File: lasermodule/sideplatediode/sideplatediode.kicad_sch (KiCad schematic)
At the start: 4 parts, among them J1 Conn_01x02

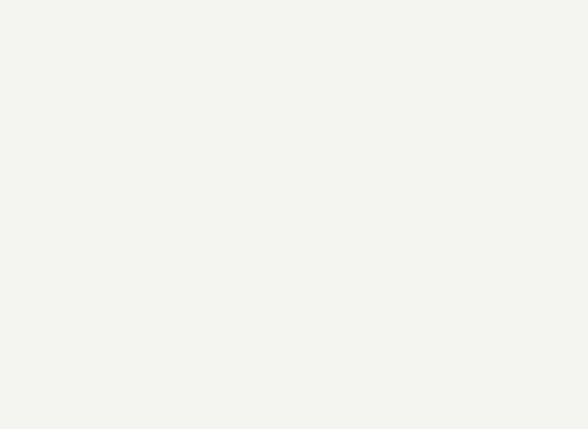
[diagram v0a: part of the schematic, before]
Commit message: removed need for screws using pcb pads
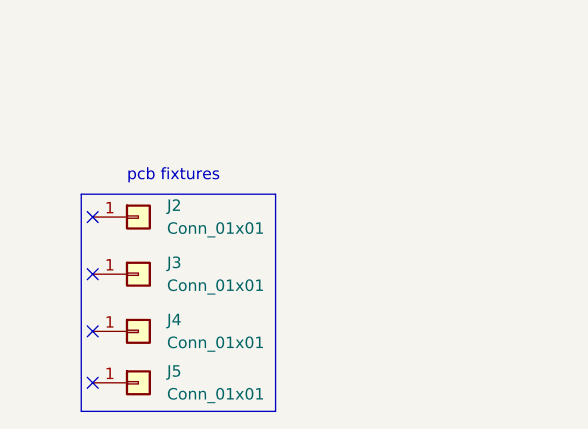
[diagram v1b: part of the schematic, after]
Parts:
- added J2, J3, J4, J5: Conn_01x01, start-of-scanline-detector:TestPoint_Pad_2.0x2.0mm_nosilk, symbol Connector_Generic:Conn_01x01
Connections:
- no-connect marks 0 -> 4
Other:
- note added: "pcb fixtures"
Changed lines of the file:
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@@
     (comment 1 "Author: Rik Starmans")
   )
+  (no_connect (at 51.435 112.395))
+  (no_connect (at 51.435 118.11))
+  (no_connect (at 51.435 106.045))
+  (no_connect (at 51.435 99.695))
+  (polyline (pts (xy 50.165 97.155) (xy 71.755 97.155))
+    (stroke (width 0) (type default))
+  )
   (wire (pts (xy 58.42 52.07) (xy 58.42 41.91))
     (stroke (width 0) (type default))
@@
     (stroke (width 0) (type default))
   )
+  (polyline (pts (xy 50.165 121.285) (xy 71.755 121.285))
+    (stroke (width 0) (type default))
+  )
   (wire (pts (xy 53.34 52.07) (xy 58.42 52.07))
     (stroke (width 0) (type default))
@@
     (stroke (width 0) (type default))
   )
+  (polyline (pts (xy 50.165 97.155) (xy 50.165 121.285))
+    (stroke (width 0) (type default))
+  )
+  (polyline (pts (xy 71.755 121.285) (xy 71.755 97.155))
+    (stroke (width 0) (type default))
+  )
   (text "back" (at 110.49 62.23 0)
+    (effects (font (size 1.27 1.27)) (justify left bottom))
+  )
+  (text "pcb fixtures" (at 55.245 95.885 0)
     (effects (font (size 1.27 1.27)) (justify left bottom))
   )
@@
     )
   )
+  (symbol (lib_id "Connector_Generic:Conn_01x01") (at 56.515 112.395 0) (unit 1)
+    (in_bom yes) (on_board yes) (dnp no) (fields_autoplaced)
+    (property "Reference" "J4" (at 59.69 111.125 0)
+      (effects (font (size 1.27 1.27)) (justify left))
+    )
+    (property "Value" "Conn_01x01" (at 59.69 113.665 0)
+      (effects (font (size 1.27 1.27)) (justify left))
+    )
+    (property "Footprint" "start-of-scanline-detector:TestPoint_Pad_2.0x2.0mm_nosilk" (at 56.515 112.395 0)
+      (effects (font (size 1.27 1.27)) hide)
+    )
+    (property "Datasheet" "~" (at 56.515 112.395 0)
+      (effects (font (size 1.27 1.27)) hide)
+    )
+    (pin "1")
+    (instances
+      (project "sideplatediode"
+        (path "/0f31f11f-c374-4640-b9a4-07bbdba8d354"
+          (reference "J4") (unit 1)
+        )
+      )
+    )
+  )
   (symbol (lib_id "Graphic:Logo_Open_Hardware_Small") (at 92.71 68.58 0) (unit 1)
     (in_bom no) (on_board yes) (dnp no) (fields_autoplaced)
@@
         )
       )
+    )
+  )
+  (symbol (lib_id "Connector_Generic:Conn_01x01") (at 56.515 118.11 0) (unit 1)
+    (in_bom yes) (on_board yes) (dnp no) (fields_autoplaced)
+    (property "Reference" "J5" (at 59.69 116.84 0)
+      (effects (font (size 1.27 1.27)) (justify left))
+    )
+    (property "Value" "Conn_01x01" (at 59.69 119.38 0)
+      (effects (font (size 1.27 1.27)) (justify left))
+    )
+    (property "Footprint" "start-of-scanline-detector:TestPoint_Pad_2.0x2.0mm_nosilk" (at 56.515 118.11 0)
+      (effects (font (size 1.27 1.27)) hide)
+    )
+    (property "Datasheet" "~" (at 56.515 118.11 0)
+      (effects (font (size 1.27 1.27)) hide)
+    )
+    (pin "1")
+    (instances
+      (project "sideplatediode"
+        (path "/0f31f11f-c374-4640-b9a4-07bbdba8d354"
+          (reference "J5") (unit 1)
+        )
+      )
+    )
+  )
+  (symbol (lib_id "Connector_Generic:Conn_01x01") (at 56.515 106.045 0) (unit 1)
+    (in_bom yes) (on_board yes) (dnp no) (fields_autoplaced)
+    (property "Reference" "J3" (at 59.69 104.775 0)
+      (effects (font (size 1.27 1.27)) (justify left))
+    )
+    (property "Value" "Conn_01x01" (at 59.69 107.315 0)
+      (effects (font (size 1.27 1.27)) (justify left))
+    )
+    (property "Footprint" "start-of-scanline-detector:TestPoint_Pad_2.0x2.0mm_nosilk" (at 56.515 106.045 0)
+      (effects (font (size 1.27 1.27)) hide)
+    )
+    (property "Datasheet" "~" (at 56.515 106.045 0)
+      (effects (font (size 1.27 1.27)) hide)
+    )
+    (pin "1")
+    (instances
+      (project "sideplatediode"
+        (path "/0f31f11f-c374-4640-b9a4-07bbdba8d354"
+          (reference "J3") (unit 1)
+        )
+      )
+    )
+  )
+  (symbol (lib_id "Connector_Generic:Conn_01x01") (at 56.515 99.695 0) (unit 1)
+    (in_bom yes) (on_board yes) (dnp no) (fields_autoplaced)
+    (property "Reference" "J2" (at 59.69 98.425 0)
+      (effects (font (size 1.27 1.27)) (justify left))
+    )
+    (property "Value" "Conn_01x01" (at 59.69 100.965 0)
+      (effects (font (size 1.27 1.27)) (justify left))
+    )
+    (property "Footprint" "start-of-scanline-detector:TestPoint_Pad_2.0x2.0mm_nosilk" (at 56.515 99.695 0)
+      (effects (font (size 1.27 1.27)) hide)
+    )
+    (property "Datasheet" "~" (at 56.515 99.695 0)
+      (effects (font (size 1.27 1.27)) hide)
+    )
+    (pin "1")
+    (instances
+      (project "sideplatediode"
+        (path "/0f31f11f-c374-4640-b9a4-07bbdba8d354"
+          (reference "J2") (unit 1)
+        )
+      )

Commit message: board almost fully synced close for release
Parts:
- removed J1: Conn_01x02, Connector_PinHeader_2.54mm:PinHeader_1x02_P2.54mm_Horizontal, symbol Connector_Generic:Conn_01x02
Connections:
- net GND: now reaches D1.A
- net GND: now also J4.1 (Pin_1)
- net DiodeK: now reaches D1.C
- net DiodeK: now also J5.1 (Pin_1)
- no-connect marks 4 -> 2
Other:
- moved on the sheet: J2, J3, J4, J5

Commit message: fixed boms, small modifications to the boards.
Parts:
- D1: MANUFACTURER OSRAM -> (none); PARTREV 1.5 -> (none); STANDARD Manufacturer Recommendations -> (none); manuf# (none) -> BPW 34 S; mouser# (none) -> 720-BPW34S-Z
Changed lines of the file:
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@@
 			)
 		)
-		(property "MANUFACTURER" "OSRAM"
+		(property "manuf#" "BPW 34 S"
 			(at 50.8 41.91 0)
 			(effects
@@
 			)
 		)
-		(property "PARTREV" "1.5"
+		(property "mouser#" "720-BPW34S-Z"
 			(at 50.8 41.91 0)
 			(effects
-				(font
-					(size 1.27 1.27)
-				)
-				(justify left bottom)
-				(hide yes)
-			)
-		)
-		(property "STANDARD" "Manufacturer Recommendations"
-			(at 50.8 41.91 0)
-			(effects
